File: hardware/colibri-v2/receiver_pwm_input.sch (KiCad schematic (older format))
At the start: 10 parts

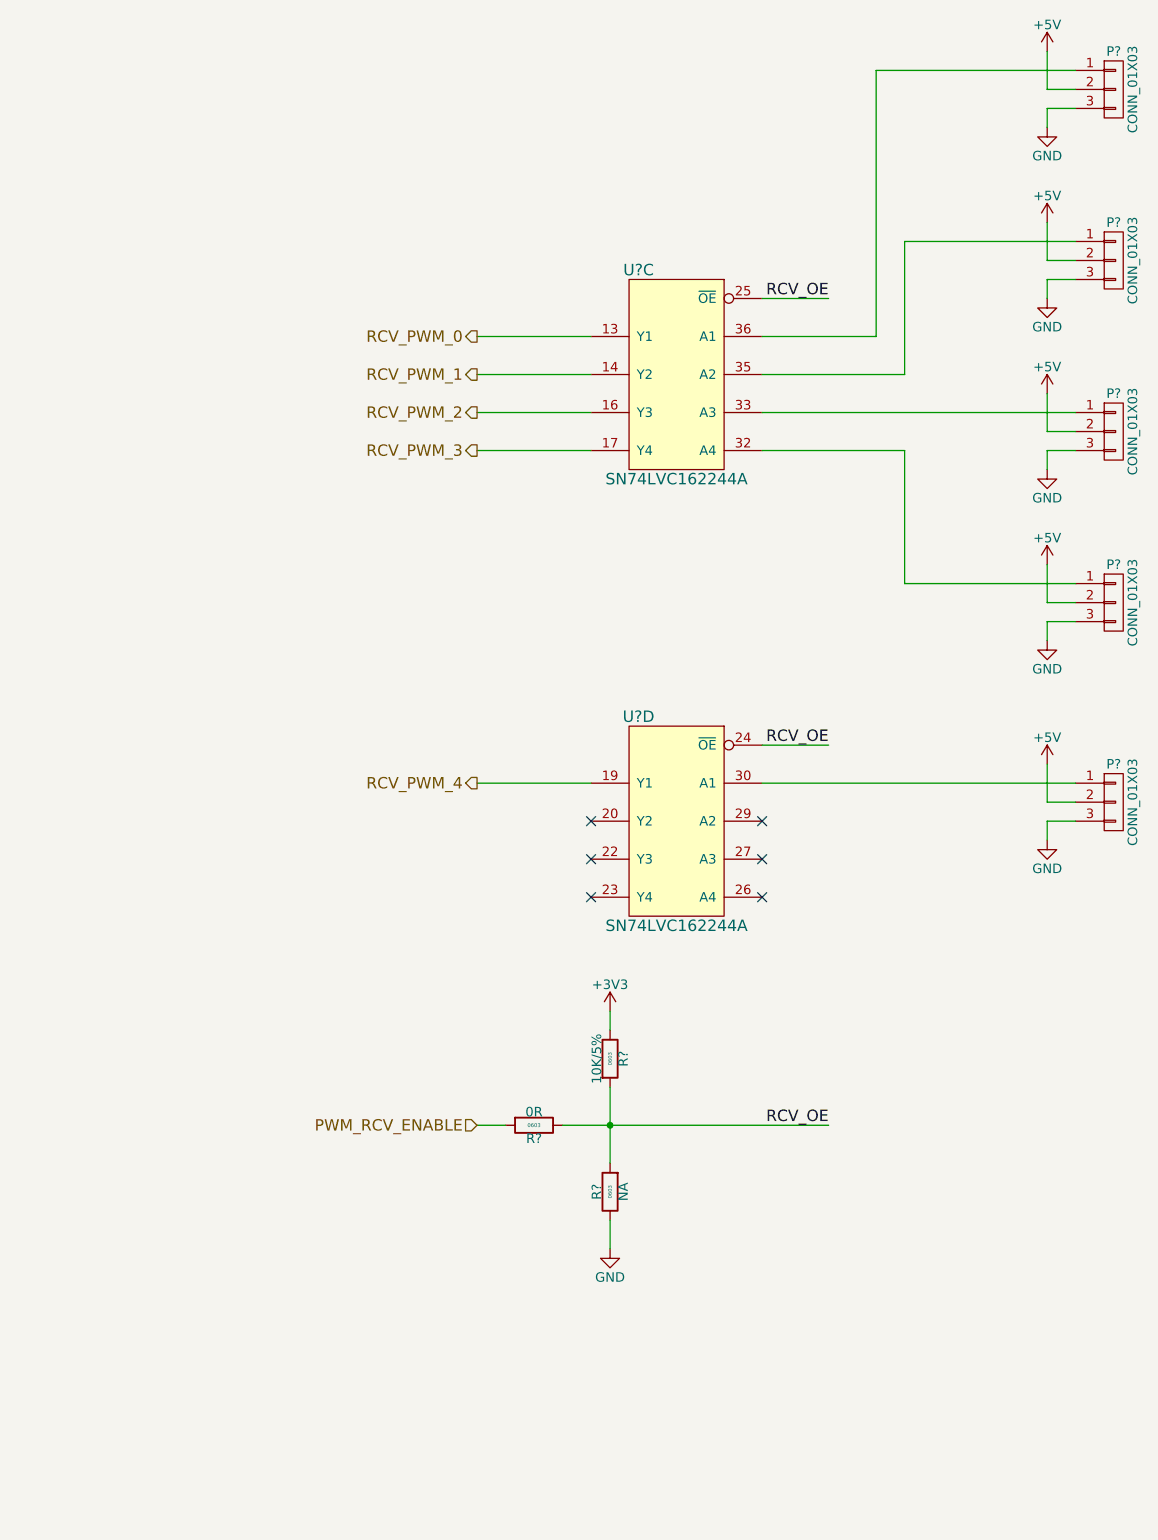
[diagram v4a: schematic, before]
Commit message: Added Power-On-Reset controller MCP120 to the Cortex
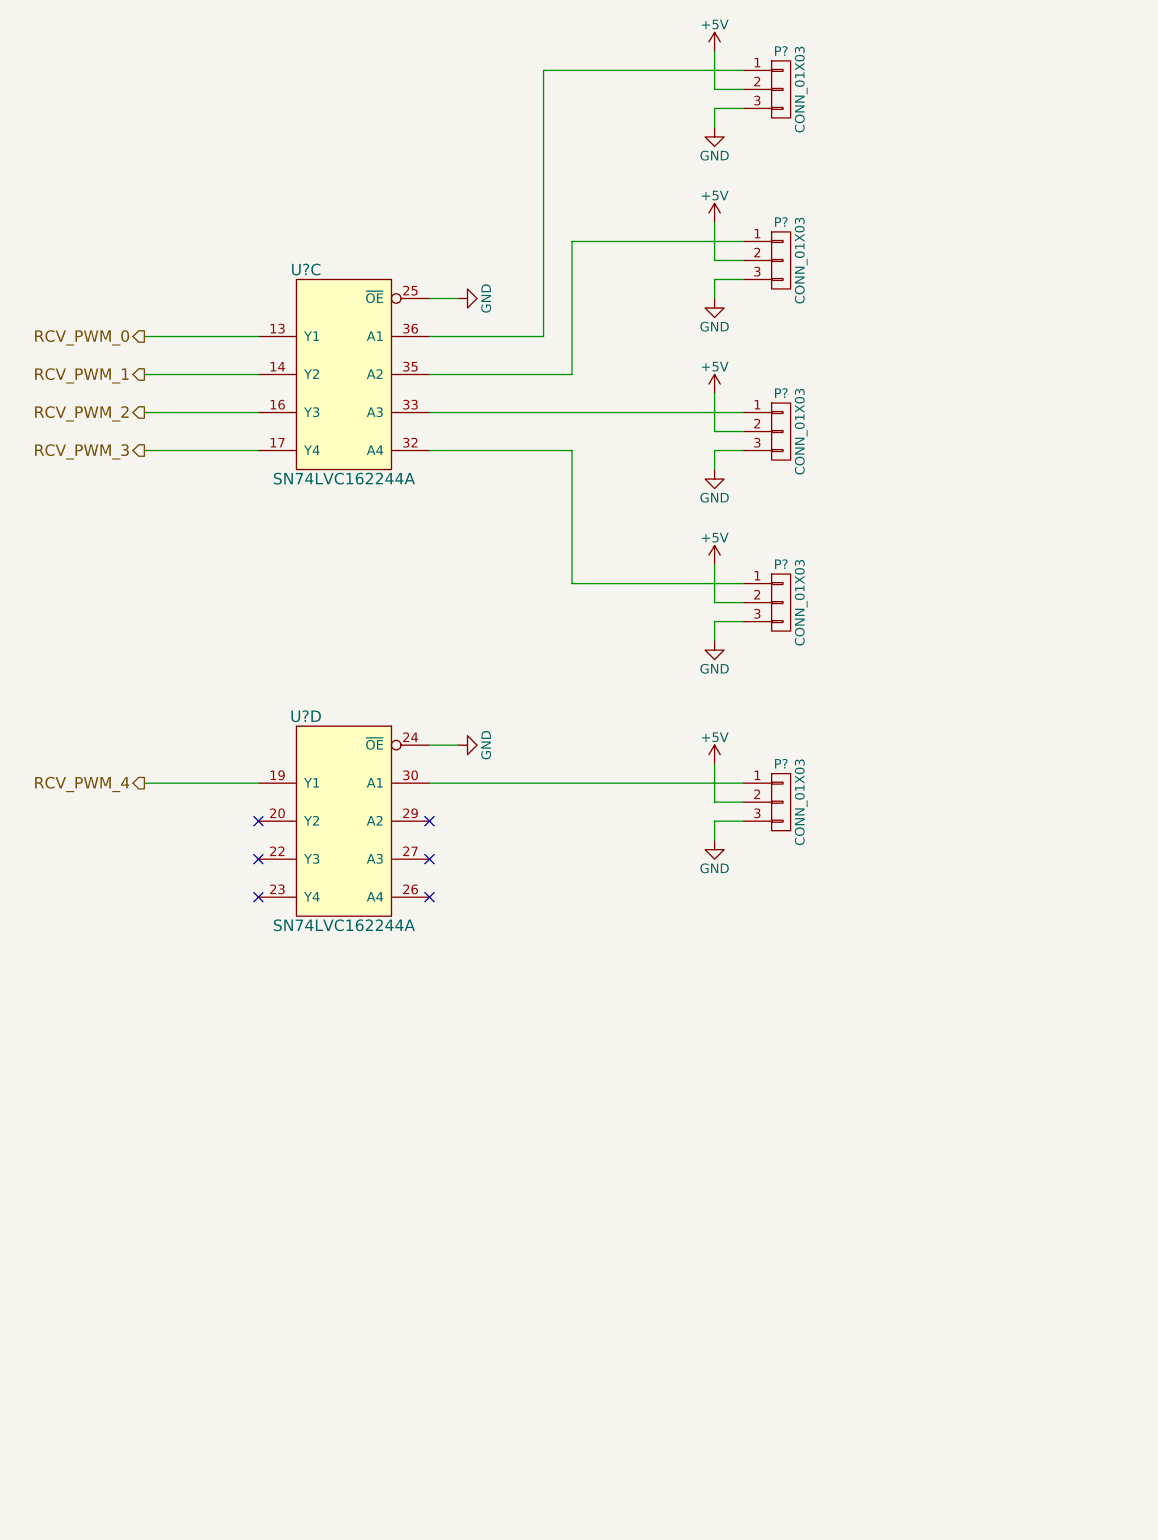
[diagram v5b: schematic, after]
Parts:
- removed R?: 10K/5%, Resistors_SMD:R_0603, symbol R_SMT
- removed R?: 0R, Resistors_SMD:R_0603, symbol R_SMT
- removed R?: NA, Resistors_SMD:R_0603, symbol R_SMT
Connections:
- net RCV_OE is gone; now on net GND: U?.24 (~OE), U?.25 (~OE)
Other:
- moved on the sheet: P?, U?C, U?D
